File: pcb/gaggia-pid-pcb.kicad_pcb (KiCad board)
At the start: 2 copper layers, 55.9 x 77.5 mm, 19 parts, among them J1 Conn_01x04, J2 Conn_01x02, J3 Conn_01x02, J4 Conn_01x02, U1 Adafruit MAX31865, U2 RP2040-ZERO

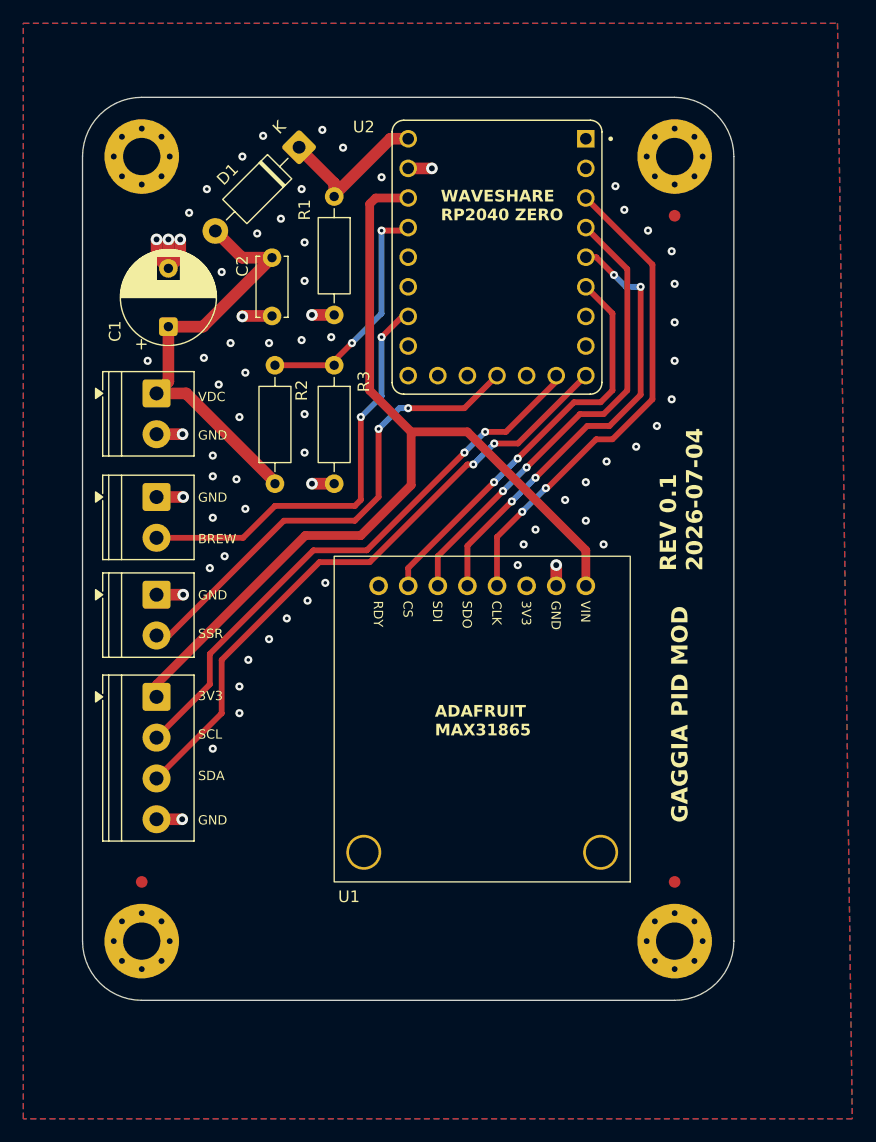
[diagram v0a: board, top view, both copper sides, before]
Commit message: Updated Vsens for PR2040-zero board
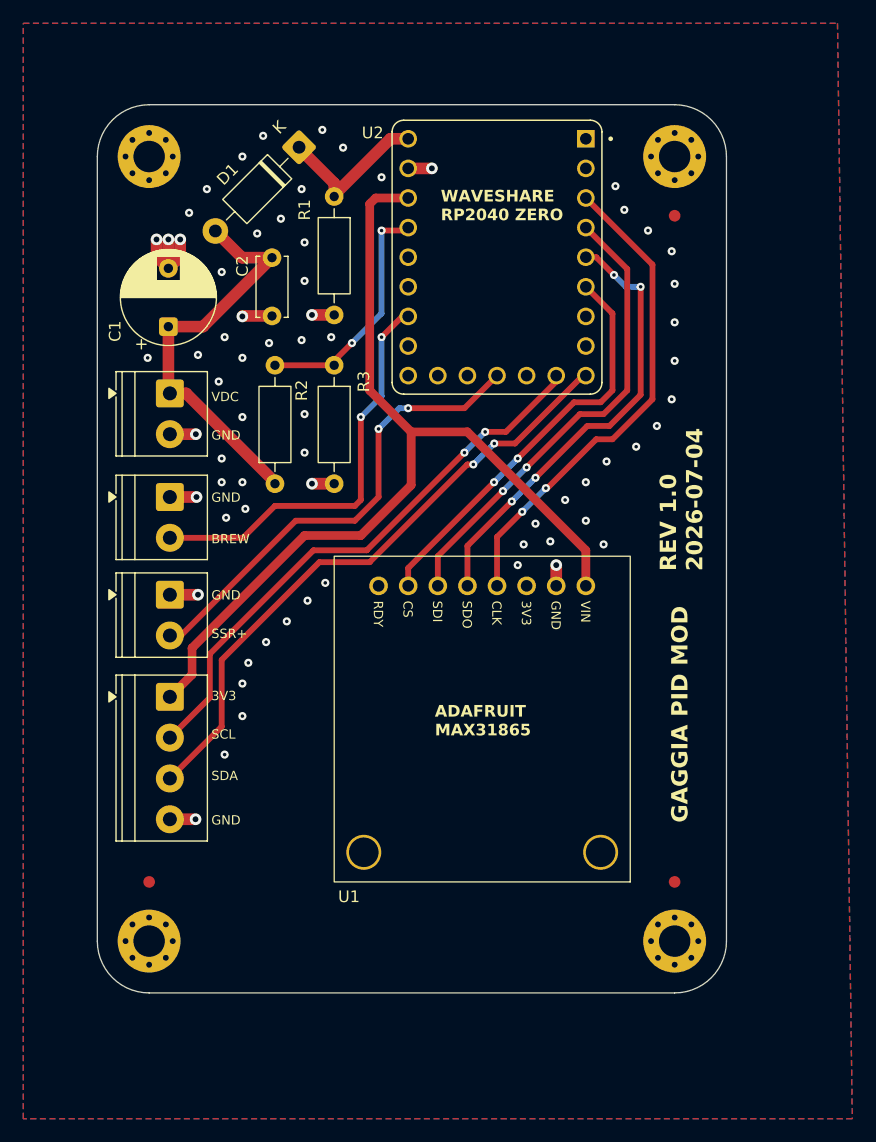
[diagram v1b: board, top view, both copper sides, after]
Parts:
- MH1, MH2, MH3, MH4: footprint MountingHole:MountingHole_3.2mm_M3_Pad_Via -> MountingHole:MountingHole_2.7mm_M2.5_Pad_Via
- moved J1 1.14 mm to (110.4, 132.7)
- moved J2 1.14 mm to (110.4, 124.0)
- moved J3 1.14 mm to (110.4, 115.6)
- moved J4 1.14 mm to (110.4, 106.7)
- moved FM2 0.63 mm to (108.6, 148.6)
- moved MH1 0.63 mm to (108.6, 86.4)
- moved MH2 0.63 mm to (108.6, 153.7)
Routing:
- net VDC: track 36.7 -> 34.2 mm
- net GPIO_BREW_SW: track 36.6 -> 35.5 mm
- net GPIO_SSR: track 41.9 -> 40.8 mm
- net GND: track 27.5 -> 27.6 mm, vias 69 -> 68
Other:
- board size 55.9 x 77.5 mm -> 54 x 76.2 mm
- board text added: "REV 1.0 2026-07-04"
- board text added: "SSR+"
- board text removed: "REV 0.1 2026-07-04"
- board text removed: "SSR"
